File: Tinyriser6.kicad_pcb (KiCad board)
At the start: 2 copper layers, 113.2 x 22 mm, 20 parts, among them J1 Bus_M.2_Socket_M, J2 Bus_PCI_Express_x16

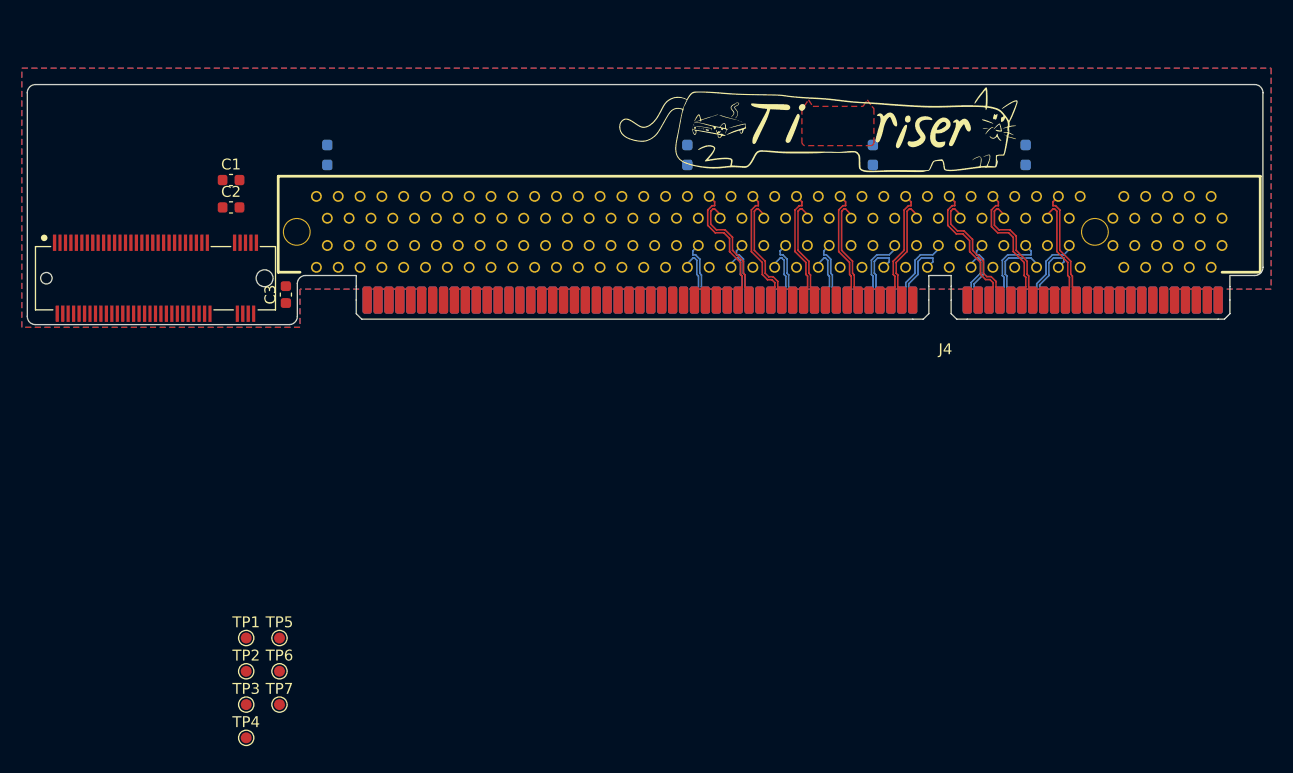
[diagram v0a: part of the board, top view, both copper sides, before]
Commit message: Imported a bunch of verified changes from Tiny5 riser v2
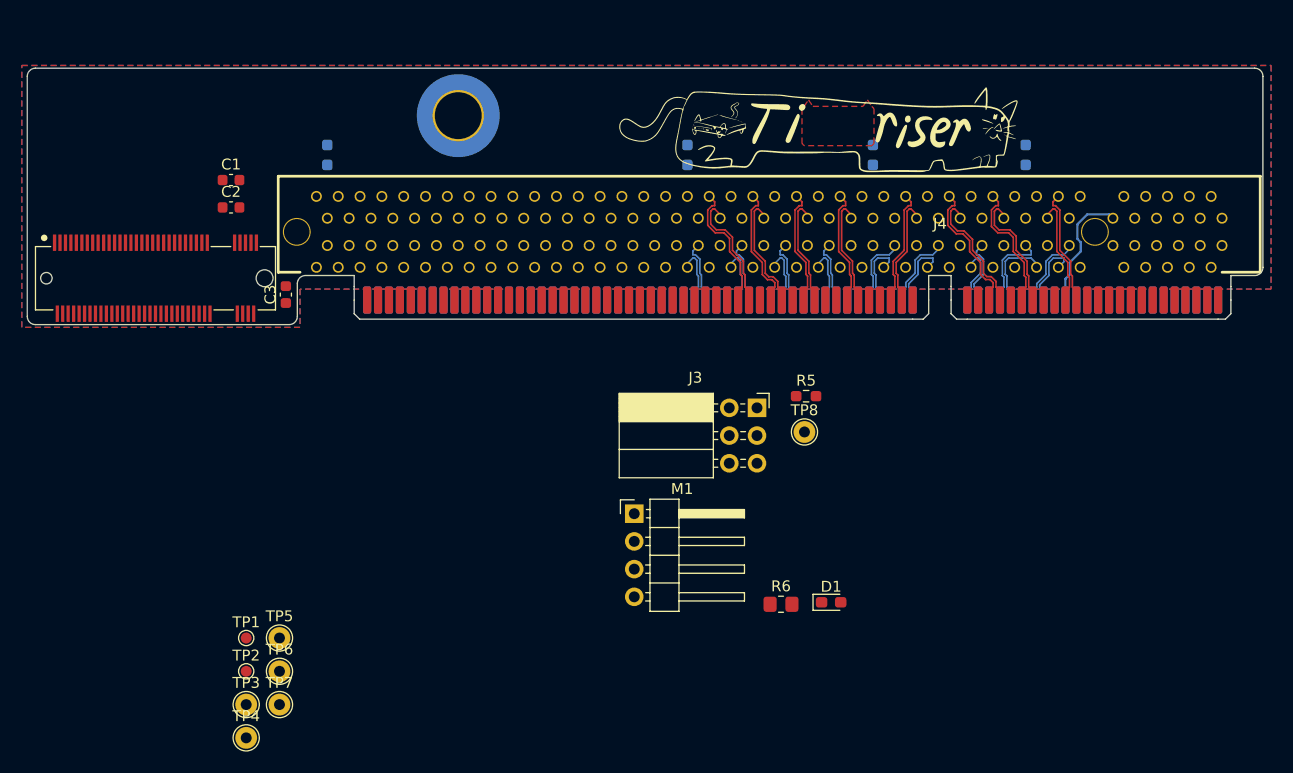
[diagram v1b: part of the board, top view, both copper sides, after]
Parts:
- added D1: LED, Diode_SMD:D_0603_1608Metric_Pad1.05x0.95mm_HandSolder, F.Cu at (194.2, 111.2)
- added H1: MountingHole_Pad, MountingHole:MountingHole_4.3mm_M4_ISO7380_Pad_TopOnly, B.Cu at (160.0, 66.6)
- added J3: fancontrol_header, Connector_PinSocket_2.54mm:PinSocket_2x03_P2.54mm_Horizontal, F.Cu at (187.4, 93.4)
- added M1: Fan_4pin, Connector_PinHeader_2.54mm:PinHeader_1x04_P2.54mm_Horizontal, F.Cu at (176.1, 103.1)
- added R5: 5K1, Resistor_SMD:R_0603_1608Metric_Pad0.98x0.95mm_HandSolder, F.Cu at (191.9, 92.3)
- added R6: 0R, Resistor_SMD:R_0805_2012Metric_Pad1.20x1.40mm_HandSolder, F.Cu at (189.6, 111.4)
- added TP8: +12V, TestPoint:TestPoint_THTPad_D2.0mm_Drill1.0mm, F.Cu at (191.7, 95.6)
- TP3, TP4, TP5, TP6, TP7: footprint TestPoint:TestPoint_Pad_D1.0mm -> TestPoint:TestPoint_THTPad_D2.0mm_Drill1.0mm
- moved J4 11.5 mm to (204.2, 77.0)
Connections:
- J1 pad 10: unconnected-(J1-DAS/~{DSS}/~{LED1}-Pad10) -> Net-(D1-K)
- J2 pad B81: Net-(J2-~{PRSNT2}-PadB81) -> PCIe_CPU_CLKREQ#
- R1 pad 2: Net-(J2-~{PRSNT2}-PadB81) -> PCIe_CPU_CLKREQ#
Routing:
- net WAKE#: track 0.00 -> 11.4 mm
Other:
- board size 113.2 x 22 mm -> 113.2 x 23.5 mm

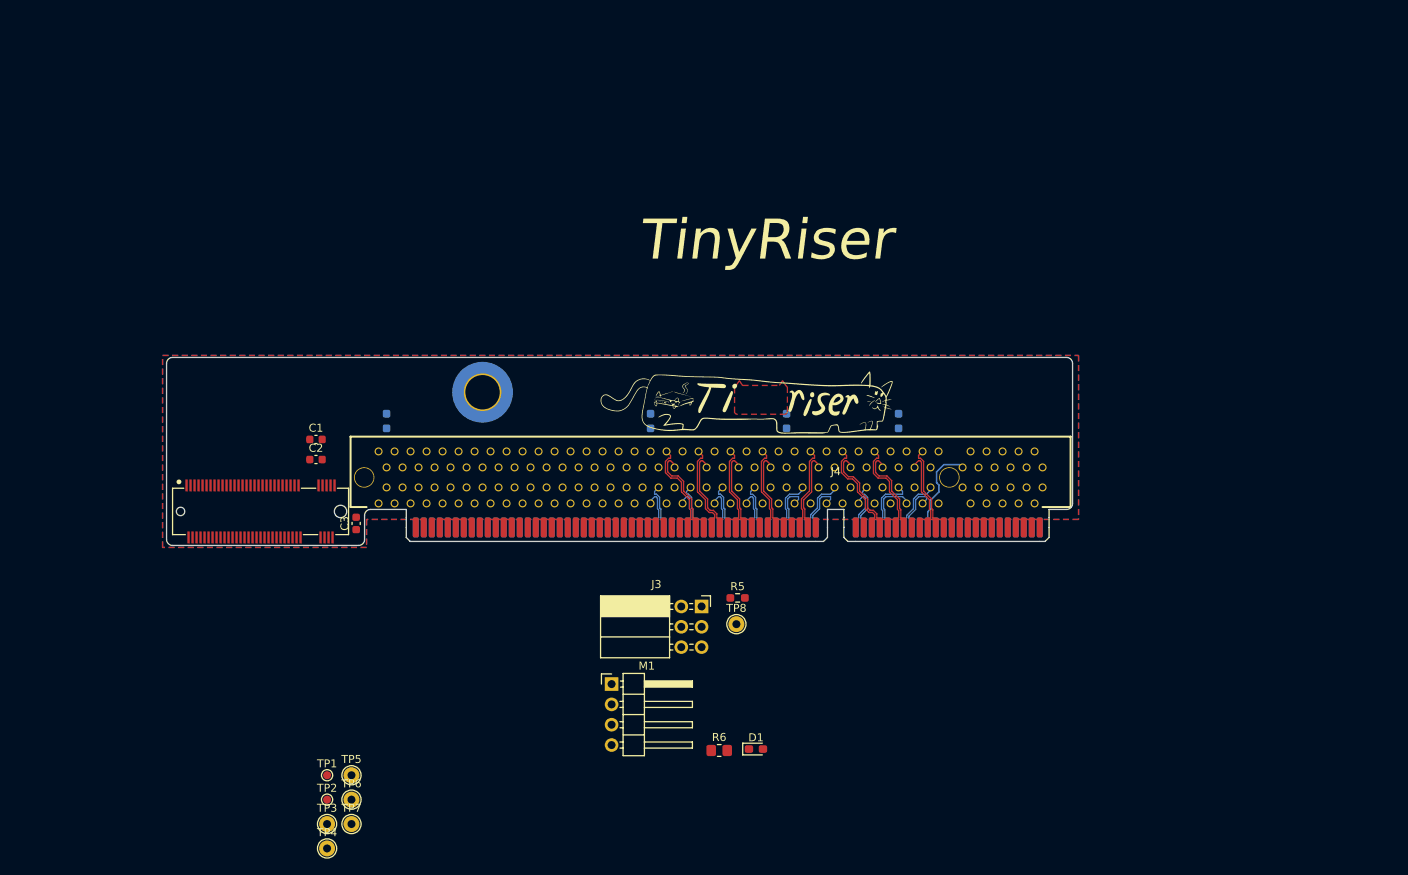
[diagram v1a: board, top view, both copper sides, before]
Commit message: carrying over a bunch of stuff from original tinyriser
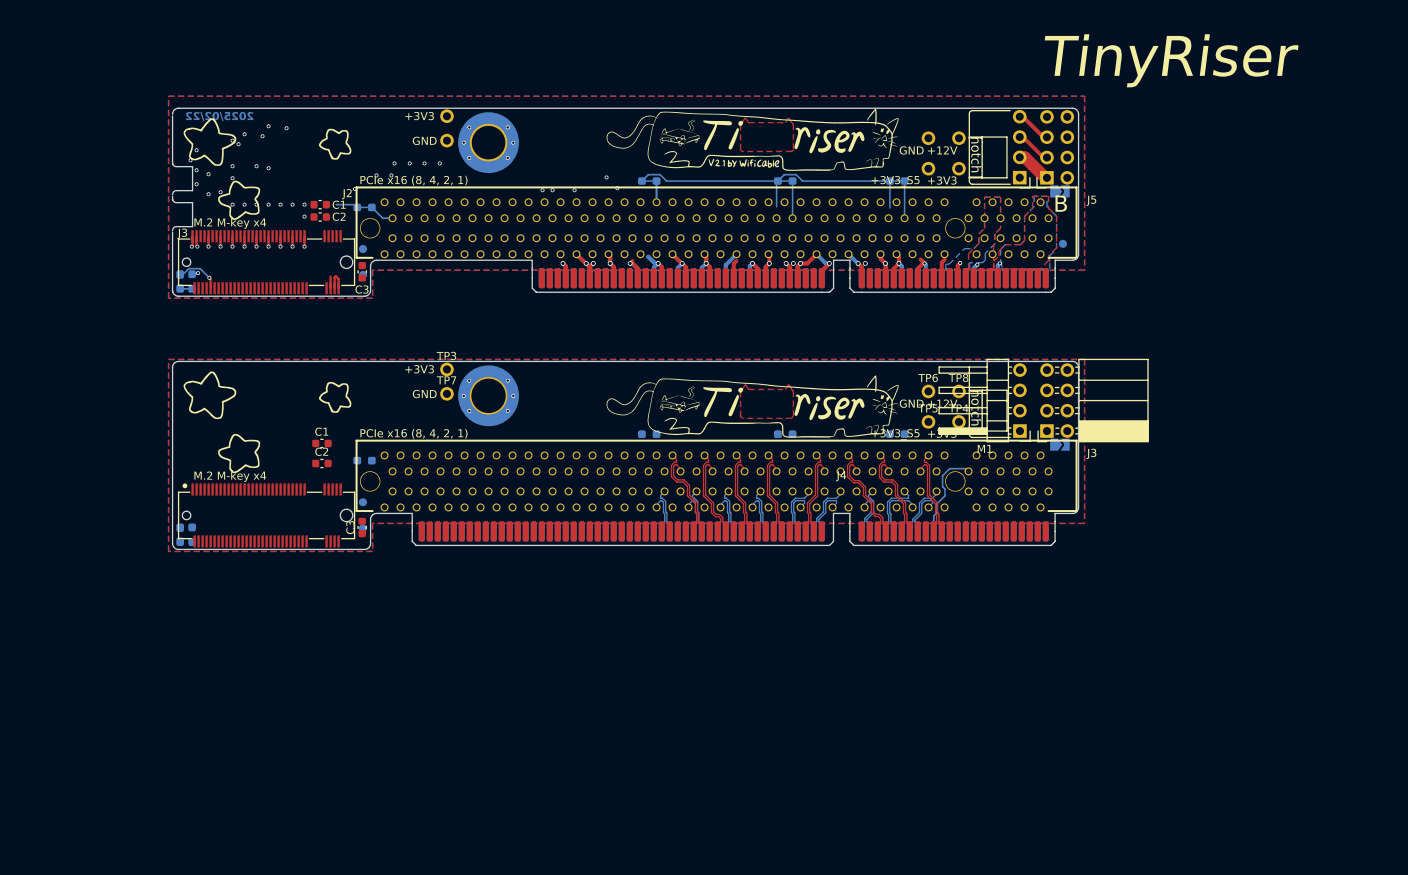
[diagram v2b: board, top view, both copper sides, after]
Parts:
- removed the G*** at (132.2, 71.1)
- removed the J3 at (187.4, 93.4)
- added C1: 10uF, Capacitor_SMD:C_0603_1608Metric, F.Cu at (139.7, 43.1)
- added C2: 100nF, Capacitor_SMD:C_0603_1608Metric, F.Cu at (139.7, 44.7)
- added C3: 10uF, Capacitor_SMD:C_0603_1608Metric, F.Cu at (144.9, 51.5)
- added D1: LED, Diode_SMD:D_0603_1608Metric_Pad1.05x0.95mm_HandSolder, B.Cu at (122.2, 52.8)
- added G***: LOGO, LOGO, B.Cu at (222.3, 37.0)
- added G***: LOGO, A_my_stuff:birb, B.Cu at (132.7, 41.1)
- added G*** (x2): LOGO, LOGO, F.Cu at (193.8, 34.6)
- added G***: LOGO, LOGO, F.Cu at (133.7, 38.6)
- added G***: LOGO, LOGO, F.Cu at (133.7, 70.2)
- added G***: LOGO, LOGO, F.Cu at (192.6, 37.9)
- added G***: LOGO, LOGO, B.Cu at (222.3, 68.7)
- added G***: LOGO, A_my_stuff:birb, B.Cu at (132.7, 72.7)
- added H1: MountingHole_Pad, MountingHole:MountingHole_4.3mm_M4_ISO7380_Pad_TopOnly, B.Cu at (160.8, 35.4)
- added J1: ~, A_my_stuff:TinyRiser, B.Cu at (205.2, 48.6)
- added J2: Bus_PCI_Express_x16, A_my_stuff:PCIe_x16_tht, F.Cu at (189.2, 46.1)
- added J3: Bus_M.2_Socket_M, A_my_stuff:M.2_NGFF_KeyM_H5.3_Vertical, F.Cu at (133.0, 50.4)
- added J3: Conn_02x04_Odd_Even, Connector_PinSocket_2.54mm:PinSocket_2x04_P2.54mm_Horizontal, F.Cu at (230.6, 71.5)
- added J5: Conn_02x04_Odd_Even, Connector_PinSocket_2.54mm:PinSocket_2x04_P2.54mm_Horizontal, F.Cu at (230.6, 39.8)
- added JP1: SolderJumper_2_Open, Jumper:SolderJumper-2_P1.3mm_Open_TrianglePad1.0x1.5mm, B.Cu at (232.2, 73.2)
- added JP1: SolderJumper_2_Open, Jumper:SolderJumper-2_P1.3mm_Open_TrianglePad1.0x1.5mm, B.Cu at (232.2, 41.5)
- added M1: Fan_4pin, Connector_PinHeader_2.54mm:PinHeader_1x04_P2.54mm_Horizontal, F.Cu at (227.2, 39.8)
- added R1: 5K1, Resistor_SMD:R_0603_1608Metric_Pad0.98x0.95mm_HandSolder, B.Cu at (123.7, 52.8)
- added R3: 0R, Resistor_SMD:R_0603_1608Metric_Pad0.98x0.95mm_HandSolder, B.Cu at (145.2, 43.5)
- added R4: 0R, Resistor_SMD:R_0603_1608Metric_Pad0.98x0.95mm_HandSolder, B.Cu at (180.8, 40.2)
- added R5: 0R, Resistor_SMD:R_0603_1608Metric_Pad0.98x0.95mm_HandSolder, B.Cu at (197.8, 40.2)
- added TP1: PCIE_SOLT_A60, TestPoint:TestPoint_Pad_D1.0mm, B.Cu at (232.6, 48.0)
- added TP2: GPU_MACO_EN, TestPoint:TestPoint_Pad_D1.0mm, B.Cu at (145.1, 52.0)
- added TP3: GPU_PWR_EN, TestPoint:TestPoint_Pad_D1.0mm, B.Cu at (145.1, 48.7)
- added TP4: +3V3, TestPoint:TestPoint_THTPad_D1.5mm_Drill0.7mm, F.Cu at (219.6, 38.7)
- added TP5: +3V3_S5, TestPoint:TestPoint_THTPad_D1.5mm_Drill0.7mm, F.Cu at (215.7, 38.7)
- added TP6: GND, TestPoint:TestPoint_THTPad_D1.5mm_Drill0.7mm, F.Cu at (215.7, 34.8)
- added TP7: GND, TestPoint:TestPoint_THTPad_D1.5mm_Drill0.7mm, F.Cu at (155.6, 35.1)
- added TP8: +3V3, TestPoint:TestPoint_THTPad_D1.5mm_Drill0.7mm, F.Cu at (155.6, 32.1)
- added TP9: +12V, TestPoint:TestPoint_THTPad_D1.5mm_Drill0.7mm, F.Cu at (219.6, 34.8)
- D1, R5, TP1, TP2: moved to B.Cu
- R6: footprint Resistor_SMD:R_0805_2012Metric_Pad1.20x1.40mm_HandSolder -> Resistor_SMD:R_0603_1608Metric_Pad0.98x0.95mm_HandSolder; moved to B.Cu
- TP3, TP4, TP5, TP6, TP7, TP8: footprint TestPoint:TestPoint_THTPad_D2.0mm_Drill1.0mm -> TestPoint:TestPoint_THTPad_D1.5mm_Drill0.7mm
- moved TP4 95.3 mm to (219.6, 70.3)
- moved TP6 88.3 mm to (215.7, 66.5)
- moved TP5 84.6 mm to (215.7, 70.3)
- moved D1 76.8 mm to (122.2, 84.4), turned to -90 degrees
- moved R6 74.6 mm to (211.8, 40.2)
- moved R5 68.6 mm to (123.7, 84.4), turned to 90 degrees
- moved M1 60.1 mm to (227.2, 71.5), turned to 180 degrees
- moved TP3 58.8 mm to (155.6, 63.8)
- moved TP7 55.1 mm to (155.6, 66.8)
- moved TP8 40.3 mm to (219.6, 66.5)
- moved TP1 34.4 mm to (145.1, 80.3), turned to 180 degrees
- moved TP2 34.2 mm to (145.1, 83.6), turned to 180 degrees
- moved R1 5.66 mm to (145.2, 75.2), turned to 0 degrees
- moved R2 1.66 mm to (180.8, 71.8), turned to 0 degrees
- moved R3 1.66 mm to (197.8, 71.8), turned to 0 degrees
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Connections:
- R6 pad 1: +12V_fan -> PCIe_CPU_CLKREQ#
- R6 pad 2: +12V -> PCIe_CPU_CLKREQ#
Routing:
- net GND: track 0.00 -> 121.1 mm, vias 0 -> 82
- net PCIe_CPU_CLKREQ#: track 0.00 -> 64.2 mm
- net Net-(D1-K): track 0.00 -> 5.79 mm, vias 0 -> 1
- net +3V3: track 0.00 -> 5.47 mm, vias 0 -> 1
- net Taco_fan: track 0.00 -> 4.46 mm
- net +12V_fan: track 0.00 -> 4.46 mm
- net PWM_fan: track 0.00 -> 4.46 mm
- net Net-(D1-A): track 0.00 -> 1.52 mm
- added copper zone on B.Cu, net +12V
- added copper zone on F.Cu, net +12V
- added copper zone on B.Cu, net +3V3
- added copper zone on F.Cu, net +3V3
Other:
- board size 113.2 x 23.5 mm -> 113.2 x 55.1 mm
- board text added: "+12V"
- board text added: "+3V3"
- board text added: "+3V3_S5"
- board text added: "12V FAN"
- board text added: "12V SYS"
- board text added: "2025/02/22"
- board text added: "3V3"
- board text added: "Compatible with Tiny5: Lenovo ThinkCentre M720q, M920q, M920x Tiny Lenovo ThinkStation P330 Tiny NEC Mate MC-3, MC-4, MC-5"
- board text added: "Fan 12V jumper"
- board text added: "GND"
- board text added: "GPU_MACO_EN"
- board text added: "GPU_PWR_EN"
- board text added: "M.2 M-key x4"
- board text added: "PCIE_SOLT_A60"
- board text added: "PCIe x16 (8, 4, 2, 1)"
- board text added: "PWM"
- board text added: "SMB CLK"
- board text added: "SMB DAT"
- board text added: "SSD Act"
- board text added: "notch"
- board text added: "x1"
- board text added: "x16"
- board text added: "x4"
- board text added: "x8"

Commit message: slightly adjusted edge connector footprint dimensions
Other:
- board text added: "Compatible with Tiny6: Lenovo ThinkCentre M90q Gen 1, M90q Gen 2 Tiny Lenovo ThinkStation P340, P350 Tiny"
